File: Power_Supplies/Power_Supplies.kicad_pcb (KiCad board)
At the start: 2 copper layers, 3 parts, among them U1 TPS62822DLC, U2 TPS62822DLC, U3 TPS82140

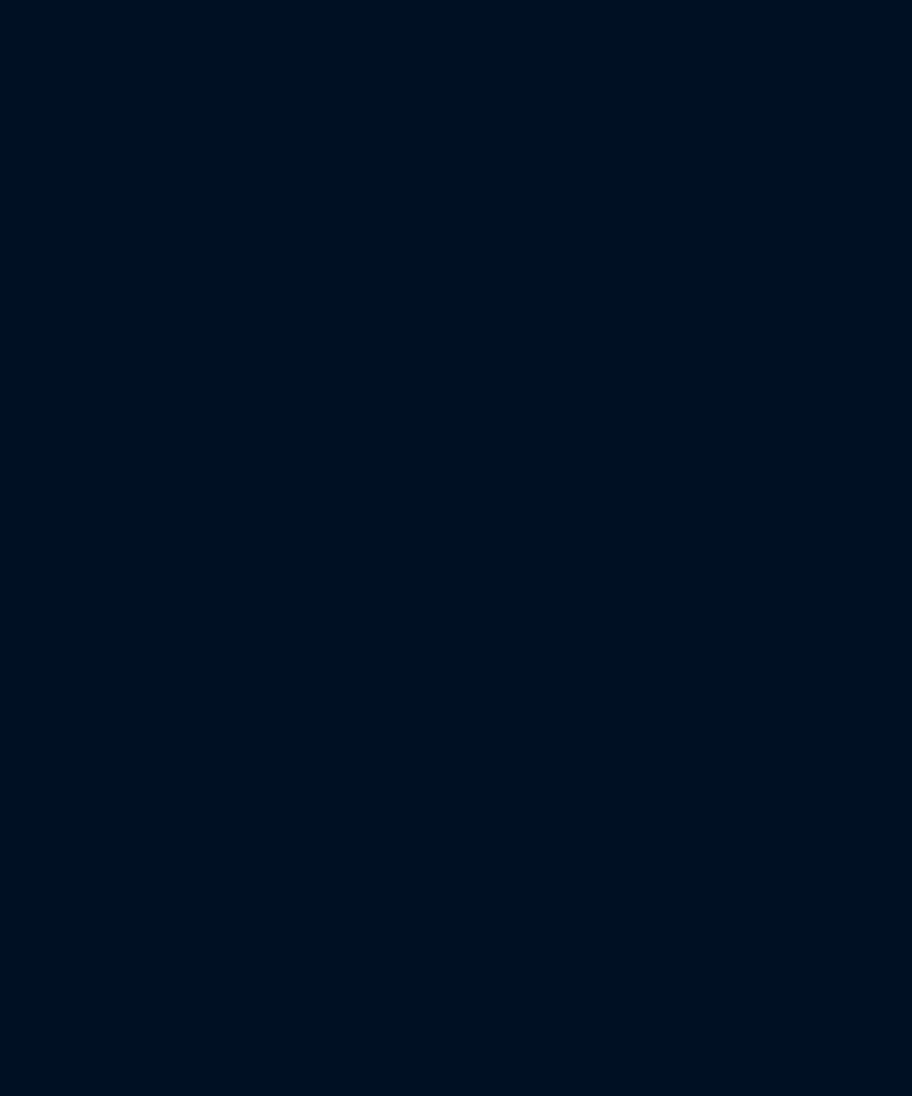
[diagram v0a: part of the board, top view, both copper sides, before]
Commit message: Added Phantom Power, updated Xcore library things
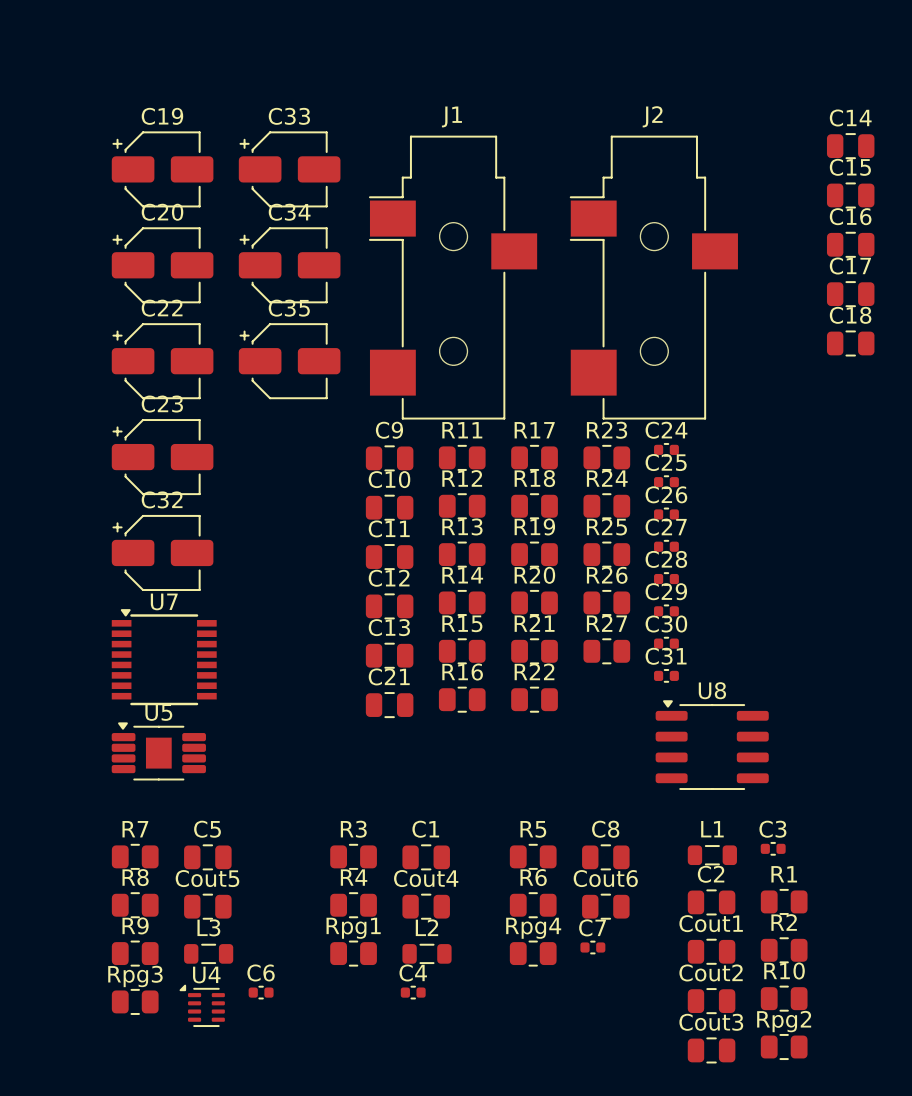
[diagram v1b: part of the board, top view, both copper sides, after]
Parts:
- added C1: 4.7uF, Capacitor_SMD:C_0805_2012Metric, F.Cu at (114.4, 85.0)
- added C10: 10uF, Capacitor_SMD:C_0805_2012Metric, F.Cu at (112.2, 63.6)
- added C11: 1uF, Capacitor_SMD:C_0805_2012Metric, F.Cu at (112.2, 66.6)
- added C12: 1uF, Capacitor_SMD:C_0805_2012Metric, F.Cu at (112.2, 69.6)
- added C13: 1uF, Capacitor_SMD:C_0805_2012Metric, F.Cu at (112.2, 72.7)
- added C14: 1uF, Capacitor_SMD:C_0805_2012Metric, F.Cu at (140.3, 41.6)
- added C15: 0.1uF, Capacitor_SMD:C_0805_2012Metric, F.Cu at (140.3, 44.6)
- added C16: 0.1uF, Capacitor_SMD:C_0805_2012Metric, F.Cu at (140.3, 47.6)
- added C17: 1uF, Capacitor_SMD:C_0805_2012Metric, F.Cu at (140.3, 50.6)
- added C18: 1uF, Capacitor_SMD:C_0805_2012Metric, F.Cu at (140.3, 53.6)
- added C19: 10uF, Capacitor_SMD:CP_Elec_4x5.8, F.Cu at (98.3, 43.0)
- added C2: 4.7uF, Capacitor_SMD:C_0805_2012Metric, F.Cu at (131.8, 87.7)
- added C20: 10uF, Capacitor_SMD:CP_Elec_4x5.8, F.Cu at (98.3, 48.8)
- added C21: 0.1uF, Capacitor_SMD:C_0805_2012Metric, F.Cu at (112.2, 75.7)
- added C22: 10uF, Capacitor_SMD:CP_Elec_4x5.8, F.Cu at (98.3, 54.7)
- added C23: 10uF, Capacitor_SMD:CP_Elec_4x5.8, F.Cu at (98.3, 60.5)
- added C24: 1200pF, Capacitor_SMD:C_0402_1005Metric, F.Cu at (129.1, 60.1)
- added C25: 1200pF, Capacitor_SMD:C_0402_1005Metric, F.Cu at (129.1, 62.1)
- added C26: 120pF, Capacitor_SMD:C_0402_1005Metric, F.Cu at (129.1, 64.0)
- added C27: 120pF, Capacitor_SMD:C_0402_1005Metric, F.Cu at (129.1, 66.0)
- added C28: 1200pF, Capacitor_SMD:C_0402_1005Metric, F.Cu at (129.1, 68.0)
- added C29: 1200pF, Capacitor_SMD:C_0402_1005Metric, F.Cu at (129.1, 69.9)
- added C3: 120pF, Capacitor_SMD:C_0402_1005Metric, F.Cu at (135.6, 84.4)
- added C30: 120pF, Capacitor_SMD:C_0402_1005Metric, F.Cu at (129.1, 71.9)
- added C31: 120pF, Capacitor_SMD:C_0402_1005Metric, F.Cu at (129.1, 73.9)
- added C32: 10uF, Capacitor_SMD:CP_Elec_4x5.8, F.Cu at (98.3, 66.4)
- added C33: 10uF, Capacitor_SMD:CP_Elec_4x5.8, F.Cu at (106.1, 43.0)
- added C34: 10uF, Capacitor_SMD:CP_Elec_4x5.8, F.Cu at (106.1, 48.8)
- added C35: 10uF, Capacitor_SMD:CP_Elec_4x5.8, F.Cu at (106.1, 54.7)
- added C4: 120pF, Capacitor_SMD:C_0402_1005Metric, F.Cu at (113.6, 93.2)
- added C5: 4.7uF, Capacitor_SMD:C_0805_2012Metric, F.Cu at (101.1, 85.0)
- added C6: 120pF, Capacitor_SMD:C_0402_1005Metric, F.Cu at (104.3, 93.2)
- added C7: 430pF, Capacitor_SMD:C_0402_1005Metric, F.Cu at (124.6, 90.5)
- added C8: 22uF, Capacitor_SMD:C_0805_2012Metric, F.Cu at (125.4, 85.0)
- added C9: 1uF, Capacitor_SMD:C_0805_2012Metric, F.Cu at (112.2, 60.6)
- added Cout1: 22uF, Capacitor_SMD:C_0805_2012Metric, F.Cu at (131.8, 90.7)
- added Cout2: 22uF, Capacitor_SMD:C_0805_2012Metric, F.Cu at (131.8, 93.7)
- added Cout3: 22uF, Capacitor_SMD:C_0805_2012Metric, F.Cu at (131.8, 96.7)
- added Cout4: 22uF, Capacitor_SMD:C_0805_2012Metric, F.Cu at (114.4, 88.0)
- added Cout5: 22uF, Capacitor_SMD:C_0805_2012Metric, F.Cu at (101.1, 88.0)
- added Cout6: 47uF, Capacitor_SMD:C_0805_2012Metric, F.Cu at (125.4, 88.0)
- added J1: Line Out, Connector_Audio:Jack_3.5mm_CUI_SJ-3523-SMT_Horizontal, F.Cu at (116.1, 49.6)
- added J2: Headphone Out, Connector_Audio:Jack_3.5mm_CUI_SJ-3523-SMT_Horizontal, F.Cu at (128.3, 49.6)
- added L1: 470nH, Inductor_SMD:L_0805_2012Metric, F.Cu at (131.9, 84.8)
- added L2: 470nH, Inductor_SMD:L_0805_2012Metric, F.Cu at (114.5, 90.8)
- added L3: 470nH, Inductor_SMD:L_0805_2012Metric, F.Cu at (101.1, 90.8)
- added R1: 453k, Resistor_SMD:R_0805_2012Metric, F.Cu at (136.2, 87.7)
- added R10: 20k, Resistor_SMD:R_0805_2012Metric, F.Cu at (136.2, 93.6)
- added R11: 82k, Resistor_SMD:R_0805_2012Metric, F.Cu at (116.6, 60.6)
- added R12: 20k, Resistor_SMD:R_0805_2012Metric, F.Cu at (116.6, 63.5)
- added R13: 82k, Resistor_SMD:R_0805_2012Metric, F.Cu at (116.6, 66.5)
- added R14: 20k, Resistor_SMD:R_0805_2012Metric, F.Cu at (116.6, 69.4)
- added R15: 82k, Resistor_SMD:R_0805_2012Metric, F.Cu at (116.6, 72.4)
- added R16: 100, Resistor_SMD:R_0805_2012Metric, F.Cu at (116.6, 75.3)
- added R17: 100, Resistor_SMD:R_0805_2012Metric, F.Cu at (121.0, 60.6)
- added R18: 100, Resistor_SMD:R_0805_2012Metric, F.Cu at (121.0, 63.5)
- added R19: 100, Resistor_SMD:R_0805_2012Metric, F.Cu at (121.0, 66.5)
- added R2: 100k, Resistor_SMD:R_0805_2012Metric, F.Cu at (136.2, 90.6)
- added R20: 8.2k, Resistor_SMD:R_0805_2012Metric, F.Cu at (121.0, 69.4)
- added R21: 1k, Resistor_SMD:R_0805_2012Metric, F.Cu at (121.0, 72.4)
- added R22: 15k, Resistor_SMD:R_0805_2012Metric, F.Cu at (121.0, 75.3)
- added R23: 100, Resistor_SMD:R_0805_2012Metric, F.Cu at (125.4, 60.6)
- added R24: 8.2k, Resistor_SMD:R_0805_2012Metric, F.Cu at (125.4, 63.5)
- added R25: 1k, Resistor_SMD:R_0805_2012Metric, F.Cu at (125.4, 66.5)
- added R26: 15k, Resistor_SMD:R_0805_2012Metric, F.Cu at (125.4, 69.4)
- added R27: 100, Resistor_SMD:R_0805_2012Metric, F.Cu at (125.4, 72.4)
- added R3: 200k, Resistor_SMD:R_0805_2012Metric, F.Cu at (110.0, 84.9)
- added R4: 100k, Resistor_SMD:R_0805_2012Metric, F.Cu at (110.0, 87.9)
- added R5: 523k, Resistor_SMD:R_0805_2012Metric, F.Cu at (120.9, 84.9)
- added R6: 100k, Resistor_SMD:R_0805_2012Metric, F.Cu at (120.9, 87.9)
- added R7: 49.9k, Resistor_SMD:R_0805_2012Metric, F.Cu at (96.7, 84.9)
- added R8: 100k, Resistor_SMD:R_0805_2012Metric, F.Cu at (96.7, 87.9)
- added R9: 10k, Resistor_SMD:R_0805_2012Metric, F.Cu at (96.7, 90.8)
- added Rpg1: 100k, Resistor_SMD:R_0805_2012Metric, F.Cu at (110.0, 90.8)
- added Rpg2: 100k, Resistor_SMD:R_0805_2012Metric, F.Cu at (136.2, 96.5)
- added Rpg3: 100k, Resistor_SMD:R_0805_2012Metric, F.Cu at (96.7, 93.8)
- added Rpg4: 100k, Resistor_SMD:R_0805_2012Metric, F.Cu at (120.9, 90.8)
- added U4: TPS62822DLC, Package_SON:Texas_VSON-HR-8_1.5x2mm_P0.5mm, F.Cu at (101.0, 94.1)
- added U5: TPA6110A2DGN, Package_SO:HVSSOP-8-1EP_3x3mm_P0.65mm_EP1.57x1.89mm, F.Cu at (98.1, 78.6)
- added U7: PCM1780, Package_SO:SSOP-16_3.9x4.9mm_P0.635mm, F.Cu at (98.4, 72.9)
- added U8: OPA2134, Package_SO:SOIC-8_3.9x4.9mm_P1.27mm, F.Cu at (131.9, 78.2)
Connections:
- net AGND renamed LEFT_IN
- U1 pad 1: 5V -> Net-(U1-EN)
- U1 pad 8: Net-(U1-PG) -> 0.9V_EN

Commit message: Add files via upload
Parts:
- removed C14, C17, C18: 1uF, Capacitor_SMD:C_0805_2012Metric
- removed C15, C16: 0.1uF, Capacitor_SMD:C_0805_2012Metric
- removed C32: 10uF, Capacitor_SMD:CP_Elec_4x5.8
- added C100: 18pF, Capacitor_SMD:C_0402_1005Metric, F.Cu at (177.9, 50.9)
- added C101: 18pF, Capacitor_SMD:C_0402_1005Metric, F.Cu at (177.9, 52.9)
- added C103: 2.2uF, Capacitor_SMD:C_0402_1005Metric, F.Cu at (210.2, 114.8)
- added C108: 2.2uF, Capacitor_SMD:C_0402_1005Metric, F.Cu at (210.2, 116.8)
- added C109: 2.2uF, Capacitor_SMD:C_0402_1005Metric, F.Cu at (210.2, 118.8)
- added C110: 47 uF, Capacitor_SMD:CP_Elec_4x5.8, F.Cu at (119.4, 27.9)
- added C111: 47 uF, Capacitor_SMD:CP_Elec_4x5.8, F.Cu at (165.5, 38.8)
- added C112: 0.1uF, Capacitor_SMD:C_0402_1005Metric, F.Cu at (160.2, 36.8)
- added C113: 0.1uF, Capacitor_SMD:C_0402_1005Metric, F.Cu at (160.2, 38.8)
- added C114: 200pF, Capacitor_SMD:C_0402_1005Metric, F.Cu at (160.2, 40.8)
- added C115: 0.1uF, Capacitor_SMD:C_0402_1005Metric, F.Cu at (160.2, 42.8)
- added C116: 10uF, Capacitor_SMD:CP_Elec_4x5.8, F.Cu at (165.5, 44.6)
- added C117: 200pF, Capacitor_SMD:C_0402_1005Metric, F.Cu at (160.2, 44.7)
- added C118: 0.1uF, Capacitor_SMD:C_0402_1005Metric, F.Cu at (160.2, 46.7)
- added C119: 0.33uF, Capacitor_SMD:C_0402_1005Metric, F.Cu at (160.2, 48.7)
- added C120: 200pF, Capacitor_SMD:C_0402_1005Metric, F.Cu at (160.2, 50.6)
- added C140: 10uF, Capacitor_SMD:CP_Elec_4x5.8, F.Cu at (176.0, 45.0)
- added C36: 0.1uF, Capacitor_SMD:C_0805_2012Metric, F.Cu at (236.5, 60.7)
- added C37: 10uF, Capacitor_SMD:CP_Elec_4x5.8, F.Cu at (191.0, 62.1)
- added C38: 0.1uF, Capacitor_SMD:C_0805_2012Metric, F.Cu at (236.5, 63.7)
- added C39: 10uF, Capacitor_SMD:CP_Elec_4x5.8, F.Cu at (191.0, 68.0)
- added C40: 0.1uF, Capacitor_SMD:C_0805_2012Metric, F.Cu at (236.5, 66.7)
- added C41: 10uF, Capacitor_SMD:CP_Elec_4x5.8, F.Cu at (191.0, 73.8)
- added C42: 1uF, Capacitor_SMD:CP_Elec_4x5.8, F.Cu at (191.0, 79.7)
- added C43: 1uF, Capacitor_SMD:CP_Elec_4x5.8, F.Cu at (191.0, 85.5)
- added C44: 0.1uF, Capacitor_SMD:C_0805_2012Metric, F.Cu at (236.5, 69.7)
- added C45: 0.1uF, Capacitor_SMD:C_0805_2012Metric, F.Cu at (236.5, 72.7)
- added C46: 10uF, Capacitor_SMD:CP_Elec_4x5.8, F.Cu at (191.0, 91.3)
- added C47: 0.1uF, Capacitor_SMD:C_0805_2012Metric, F.Cu at (236.5, 75.7)
- added C48: 10uF, Capacitor_SMD:CP_Elec_4x5.8, F.Cu at (191.0, 97.2)
- added C49: 10uF, Capacitor_SMD:CP_Elec_4x5.8, F.Cu at (191.0, 103.0)
- added C50: 1uF, Capacitor_SMD:CP_Elec_4x5.8, F.Cu at (191.0, 108.9)
- added C51: 1uF, Capacitor_SMD:CP_Elec_4x5.8, F.Cu at (198.7, 62.1)
- added C52: 0.1uF, Capacitor_SMD:C_0805_2012Metric, F.Cu at (236.5, 78.7)
- added C53: 0.1uF, Capacitor_SMD:C_0805_2012Metric, F.Cu at (241.0, 60.7)
- added C54: 10uF, Capacitor_SMD:CP_Elec_4x5.8, F.Cu at (198.7, 68.0)
- added C55: 0.1uF, Capacitor_SMD:C_0805_2012Metric, F.Cu at (241.0, 63.7)
- added C56: 10uF, Capacitor_SMD:CP_Elec_4x5.8, F.Cu at (198.7, 73.8)
- added C57: 10uF, Capacitor_SMD:CP_Elec_4x5.8, F.Cu at (198.7, 79.7)
- added C58: 1uF, Capacitor_SMD:CP_Elec_4x5.8, F.Cu at (198.7, 85.5)
- added C59: 1uF, Capacitor_SMD:CP_Elec_4x5.8, F.Cu at (198.7, 91.3)
- added C60: 0.1uF, Capacitor_SMD:C_0805_2012Metric, F.Cu at (241.0, 66.7)
- added C61: 0.1uF, Capacitor_SMD:C_0805_2012Metric, F.Cu at (241.0, 69.7)
- added C62: 10uF, Capacitor_SMD:CP_Elec_4x5.8, F.Cu at (198.7, 97.2)
- added C63: 0.1uF, Capacitor_SMD:C_0805_2012Metric, F.Cu at (241.0, 72.7)
- added C64: 10uF, Capacitor_SMD:CP_Elec_4x5.8, F.Cu at (198.7, 103.0)
- added C65: 10uF, Capacitor_SMD:CP_Elec_4x5.8, F.Cu at (198.7, 108.9)
- added C66: 1uF, Capacitor_SMD:CP_Elec_4x5.8, F.Cu at (206.5, 62.1)
- added C67: 1uF, Capacitor_SMD:CP_Elec_4x5.8, F.Cu at (206.5, 68.0)
- added C68: 0.1uF, Capacitor_SMD:C_0805_2012Metric, F.Cu at (241.0, 75.7)
- added C69: 0.1uF, Capacitor_SMD:C_0805_2012Metric, F.Cu at (241.0, 78.7)
- added C70: 10uF, Capacitor_SMD:CP_Elec_4x5.8, F.Cu at (206.5, 73.8)
- added C71: 0.1uF, Capacitor_SMD:C_0805_2012Metric, F.Cu at (241.3, 5.08)
- added C72: 10uF, Capacitor_SMD:CP_Elec_4x5.8, F.Cu at (206.5, 79.7)
- added C73: 10uF, Capacitor_SMD:CP_Elec_4x5.8, F.Cu at (206.5, 85.5)
- added C74: 1uF, Capacitor_SMD:CP_Elec_4x5.8, F.Cu at (206.5, 91.3)
- added C75: 1uF, Capacitor_SMD:CP_Elec_4x5.8, F.Cu at (206.5, 97.2)
- added C76: 0.1uF, Capacitor_SMD:C_0805_2012Metric, F.Cu at (245.4, 63.7)
- added C77: 0.1uF, Capacitor_SMD:C_0805_2012Metric, F.Cu at (245.4, 66.7)
- added C78: 10uF, Capacitor_SMD:CP_Elec_4x5.8, F.Cu at (206.5, 103.0)
- added C79: 0.1uF, Capacitor_SMD:C_0805_2012Metric, F.Cu at (245.4, 69.7)
- added C80: 10uF, Capacitor_SMD:CP_Elec_4x5.8, F.Cu at (206.5, 108.9)
- added C81: 10uF, Capacitor_SMD:CP_Elec_4x5.8, F.Cu at (214.2, 62.1)
- added C82: 1uF, Capacitor_SMD:CP_Elec_4x5.8, F.Cu at (214.2, 68.0)
- added C83: 1uF, Capacitor_SMD:CP_Elec_4x5.8, F.Cu at (214.2, 73.8)
- added C84: 0.1uF, Capacitor_SMD:C_0805_2012Metric, F.Cu at (245.4, 72.7)
- added C85: 0.1uF, Capacitor_SMD:C_0805_2012Metric, F.Cu at (245.4, 75.7)
- added C86: 10uF, Capacitor_SMD:CP_Elec_4x5.8, F.Cu at (214.2, 79.7)
- added C87: 0.1uF, Capacitor_SMD:C_0805_2012Metric, F.Cu at (245.4, 78.7)
- added C88: 10uF, Capacitor_SMD:CP_Elec_4x5.8, F.Cu at (214.2, 85.5)
- added C89: 10uF, Capacitor_SMD:CP_Elec_4x5.8, F.Cu at (214.2, 91.3)
- added C90: 1uF, Capacitor_SMD:CP_Elec_4x5.8, F.Cu at (214.2, 97.2)
- added C91: 1uF, Capacitor_SMD:CP_Elec_4x5.8, F.Cu at (214.2, 103.0)
- added C92: 0.1uF, Capacitor_SMD:C_0805_2012Metric, F.Cu at (249.9, 60.7)
- added C93: 0.1uF, Capacitor_SMD:C_0805_2012Metric, F.Cu at (249.9, 63.7)
- added C94: 10uF, Capacitor_SMD:CP_Elec_4x5.8, F.Cu at (214.2, 108.9)
- added C95: 0.1uF, Capacitor_SMD:C_0805_2012Metric, F.Cu at (249.9, 66.7)
- added C96: 10uF, Capacitor_SMD:CP_Elec_4x5.8, F.Cu at (222.0, 62.1)
- added C97: 10uF, Capacitor_SMD:CP_Elec_4x5.8, F.Cu at (222.0, 68.0)
- added C98: 1uF, Capacitor_SMD:CP_Elec_4x5.8, F.Cu at (222.0, 73.8)
- added C99: 1uF, Capacitor_SMD:CP_Elec_4x5.8, F.Cu at (222.0, 79.7)
- added D2: LED, LED_SMD:LED_0201_0603Metric, F.Cu at (165.1, 64.4)
- added DZ10: 10V, Diode_SMD:D_SMB, F.Cu at (154.6, 44.2)
- added DZ11: 10V, Diode_SMD:D_SMB, F.Cu at (154.6, 49.7)
- added DZ12: 10V, Diode_SMD:D_SMB, F.Cu at (154.6, 55.3)
- added DZ9: 10V, Diode_SMD:D_SMB, F.Cu at (154.6, 38.6)
- added IC1: PCM1808PWRG4, SamacSys_Parts:SOP65P640X120-14N, F.Cu at (230.1, 62.3)
- added IC2: PCM1808PWRG4, SamacSys_Parts:SOP65P640X120-14N, F.Cu at (230.1, 68.5)
- added IC3: PCM1808PWRG4, SamacSys_Parts:SOP65P640X120-14N, F.Cu at (230.1, 74.8)
- added IC4: PCM1808PWRG4, SamacSys_Parts:SOP65P640X120-14N, F.Cu at (230.1, 81.0)
- added IC5: PCM1808PWRG4, SamacSys_Parts:SOP65P640X120-14N, F.Cu at (230.1, 87.2)
- added IC6: PCM1808PWRG4, SamacSys_Parts:SOP65P640X120-14N, F.Cu at (230.1, 93.4)
- added IC7: PCM1808PWRG4, SamacSys_Parts:SOP65P640X120-14N, F.Cu at (230.1, 99.7)
- added IC8: PCM1808PWRG4, SamacSys_Parts:SOP65P640X120-14N, F.Cu at (230.1, 105.9)
- added IC9: LT8338, SamacSys_Parts:SOP65P490X110-9N, F.Cu at (175.6, 60.0)
- added J6: XLR3_AudioJack2_Combo, SamacSys_Parts:FA-238_EPS, F.Cu at (167.5, 60.9)
- added L4: 10uH, Inductor_SMD:L_0805_2012Metric, F.Cu at (211.0, 121.1)
- added R28: 1M, Resistor_SMD:R_0805_2012Metric, F.Cu at (174.3, 51.4)
- added R29: 10K, Resistor_SMD:R_0805_2012Metric, F.Cu at (174.3, 54.4)
- added R34: 1M, Resistor_SMD:R_0805_2012Metric, F.Cu at (202.1, 118.2)
- added R35: 162k, Resistor_SMD:R_0805_2012Metric, F.Cu at (202.1, 121.2)
- added R42: 301k, Resistor_SMD:R_0805_2012Metric, F.Cu at (206.5, 115.3)
- added R43: 1M, Resistor_SMD:R_0805_2012Metric, F.Cu at (206.5, 118.2)
- added R44: 40.2k, Resistor_SMD:R_0805_2012Metric, F.Cu at (206.5, 121.2)
- added R46: 2.2k, Resistor_SMD:R_0805_2012Metric, F.Cu at (152.6, 59.5)
- added R47: 5.1k, Resistor_SMD:R_0805_2012Metric, F.Cu at (152.6, 62.5)
- added R48: 2.2k, Resistor_SMD:R_0805_2012Metric, F.Cu at (152.6, 65.4)
- added R49: 2.2k, Resistor_SMD:R_0805_2012Metric, F.Cu at (152.6, 68.4)
- added R50: 330, Resistor_SMD:R_0805_2012Metric, F.Cu at (157.0, 59.5)
- added R51: 1M, Resistor_SMD:R_0805_2012Metric, F.Cu at (157.0, 62.5)
- added R52: 22K, Resistor_SMD:R_0805_2012Metric, F.Cu at (157.0, 65.4)
- added R53: 2.2K, Resistor_SMD:R_0805_2012Metric, F.Cu at (157.0, 68.4)
- added R54: 2.2K, Resistor_SMD:R_0805_2012Metric, F.Cu at (161.4, 59.5)
- added R55: 2.2k, Resistor_SMD:R_0805_2012Metric, F.Cu at (161.4, 62.5)
- added R56: 5.1k, Resistor_SMD:R_0805_2012Metric, F.Cu at (161.4, 65.4)
- added R60: 2.2k, Resistor_SMD:R_0805_2012Metric, F.Cu at (161.4, 68.4)
- added RV1: 10k, Potentiometer_THT:Potentiometer_ACP_CA9-V10_Vertical, F.Cu at (138.4, 44.0)
- added RV2: 10k, Potentiometer_THT:Potentiometer_ACP_CA9-V10_Vertical, F.Cu at (138.4, 55.4)
- added SW2: SW_Push, Button_Switch_THT:SW_PUSH_1P1T_6x3.5mm_H5.0_APEM_MJTP1250, F.Cu at (138.3, 61.2)
- added U10: XU316-1024-TQ128-I24, SamacSys_Parts:TQFP128_196X196_XMO, F.Cu at (224.9, 123.2)
- added U11: W25Q64JVSSIQ (FLASH MEMORY), SamacSys_Parts:SOIC-8_5P28X5P28_WIN, F.Cu at (220.8, 136.0)
- added U12: SSM2019BRNZ, SamacSys_Parts:SOIC127P600X175-8N, F.Cu at (140.5, 66.9)
- added U13: OPA2134, Package_SO:SOIC-8_3.9x4.9mm_P1.27mm, F.Cu at (165.9, 50.9)
- added U9: MAX1044, SamacSys_Parts:SOIC127P600X175-8N, F.Cu at (176.2, 39.0)
- added X1: FA-238 24.0000MB-C0 (CRYSTAL), SamacSys_Parts:FA-238_EPS, F.Cu at (229.9, 135.4)
- moved J2 143.9 mm to (266.7, 10.2)
- moved J1 141.0 mm to (251.5, 10.1)
- moved U3 82.7 mm to (51.9, 67.6)
- moved R20 65.4 mm to (65.1, 35.6)
- moved C28 64.3 mm to (68.6, 46.2), turned to 90 degrees
- moved C24 63.7 mm to (68.6, 40.2), turned to -90 degrees
- moved C29 62.6 mm to (71.1, 46.2), turned to 90 degrees
- moved U8 62.6 mm to (83.8, 38.1)
- moved C25 61.9 mm to (71.1, 40.2), turned to -90 degrees
- moved R21 58.7 mm to (75.3, 35.6)
- moved R25 54.9 mm to (74.6, 45.7)
- moved U1 54.2 mm to (56.6, 31.2)
- moved U2 54.2 mm to (50.6, 31.2)
- moved C30 52.7 mm to (91.0, 35.6)
- moved C31 52.3 mm to (91.0, 38.1)
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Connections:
- C6 pad 1: 1.8V -> 0.9V
- Cout5 pad 1: 1.8V -> 0.9V
- L3 pad 2: 1.8V -> 0.9V
- R7 pad 1: 1.8V -> 0.9V
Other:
- copper layers 2 -> 4

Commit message: Add files via upload
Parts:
- removed C100, C101: 18pF, Capacitor_SMD:C_0402_1005Metric
- removed C103, C108, C109: 2.2uF, Capacitor_SMD:C_0402_1005Metric
- removed C110, C111: 47 uF, Capacitor_SMD:CP_Elec_4x5.8
- removed C112, C113, C115, C118: 0.1uF, Capacitor_SMD:C_0402_1005Metric
- removed C114, C117, C120: 200pF, Capacitor_SMD:C_0402_1005Metric
- removed C116, C140, C37, C39, C41, C46, C48, C49, C54, C56, C57, C62, C64, C65, C70, C72, C73, C78, C80, C81, C86, C88, C89, C94, C96, C97: 10uF, Capacitor_SMD:CP_Elec_4x5.8
- removed C119: 0.33uF, Capacitor_SMD:C_0402_1005Metric
- removed C36, C38, C40, C44, C45, C47, C52, C53, C55, C60, C61, C63, C68, C69, C71, C76, C77, C79, C84, C85, C87, C92, C93, C95: 0.1uF, Capacitor_SMD:C_0805_2012Metric
- removed C42, C43, C50, C51, C58, C59, C66, C67, C74, C75, C82, C83, C90, C91, C98, C99: 1uF, Capacitor_SMD:CP_Elec_4x5.8
- removed D2: LED, LED_SMD:LED_0201_0603Metric
- removed DZ10, DZ11, DZ12, DZ9: 10V, Diode_SMD:D_SMB
- removed IC1, IC2, IC3, IC4, IC5, IC6, IC7, IC8: PCM1808PWRG4, SamacSys_Parts:SOP65P640X120-14N
- removed IC9: LT8338, SamacSys_Parts:SOP65P490X110-9N
- removed J6: XLR3_AudioJack2_Combo, SamacSys_Parts:FA-238_EPS
- removed L4: 10uH, Inductor_SMD:L_0805_2012Metric
- removed R28, R34, R43, R51: 1M, Resistor_SMD:R_0805_2012Metric
- removed R29: 10K, Resistor_SMD:R_0805_2012Metric
- removed R35: 162k, Resistor_SMD:R_0805_2012Metric
- removed R42: 301k, Resistor_SMD:R_0805_2012Metric
- removed R44: 40.2k, Resistor_SMD:R_0805_2012Metric
- removed R46, R48, R49, R55, R60: 2.2k, Resistor_SMD:R_0805_2012Metric
- removed R47, R56: 5.1k, Resistor_SMD:R_0805_2012Metric
- removed R50: 330, Resistor_SMD:R_0805_2012Metric
- removed R52: 22K, Resistor_SMD:R_0805_2012Metric
- removed R53, R54: 2.2K, Resistor_SMD:R_0805_2012Metric
- removed RV1, RV2: 10k, Potentiometer_THT:Potentiometer_ACP_CA9-V10_Vertical
- removed SW2: SW_Push, Button_Switch_THT:SW_PUSH_1P1T_6x3.5mm_H5.0_APEM_MJTP1250
- removed U10: XU316-1024-TQ128-I24, SamacSys_Parts:TQFP128_196X196_XMO
- removed U11: W25Q64JVSSIQ (FLASH MEMORY), SamacSys_Parts:SOIC-8_5P28X5P28_WIN
- removed U12: SSM2019BRNZ, SamacSys_Parts:SOIC127P600X175-8N
- removed U13: OPA2134, Package_SO:SOIC-8_3.9x4.9mm_P1.27mm
- removed U9: MAX1044, SamacSys_Parts:SOIC127P600X175-8N
- removed X1: FA-238 24.0000MB-C0 (CRYSTAL), SamacSys_Parts:FA-238_EPS
- added C14: 1uF, Capacitor_SMD:C_0805_2012Metric, F.Cu at (140.3, 41.6)
- added C15: 0.1uF, Capacitor_SMD:C_0805_2012Metric, F.Cu at (140.3, 44.6)
- added C16: 0.1uF, Capacitor_SMD:C_0805_2012Metric, F.Cu at (140.3, 47.6)
- added C17: 1uF, Capacitor_SMD:C_0805_2012Metric, F.Cu at (140.3, 50.6)
- added C18: 1uF, Capacitor_SMD:C_0805_2012Metric, F.Cu at (140.3, 53.6)
- added C32: 10uF, Capacitor_SMD:CP_Elec_4x5.8, F.Cu at (98.3, 66.4)
- moved J2 143.9 mm to (128.3, 49.6)
- moved J1 141.0 mm to (116.1, 49.6)
- moved U3 82.7 mm to (1.87, 1.77)
- moved R20 65.4 mm to (121.0, 69.4)
- moved C28 64.3 mm to (129.1, 68.0), turned to 0 degrees
- moved C24 63.7 mm to (129.1, 60.1), turned to 0 degrees
- moved C29 62.6 mm to (129.1, 69.9), turned to 0 degrees
- moved U8 62.6 mm to (131.9, 78.2)
- moved C25 61.9 mm to (129.1, 62.1), turned to 0 degrees
- moved R21 58.7 mm to (121.0, 72.4)
- moved R25 54.9 mm to (125.4, 66.5)
- moved U1 54.2 mm to (7.68, 7.94)
- moved U2 54.2 mm to (1.64, 7.94)
- moved C30 52.7 mm to (129.1, 71.9)
- moved C31 52.3 mm to (129.1, 73.9)
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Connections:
- C6 pad 1: 0.9V -> 1.8V
- Cout5 pad 1: 0.9V -> 1.8V
- L3 pad 2: 0.9V -> 1.8V
- R7 pad 1: 0.9V -> 1.8V
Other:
- copper layers 4 -> 2
